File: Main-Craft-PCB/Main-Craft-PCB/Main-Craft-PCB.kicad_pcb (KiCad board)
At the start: 2 copper layers, 220 parts, among them J1 UART_1, J10 SOL_2, J11 PWR_IN, J12 SOL_3, J13 SOL_4, J14 Conn_01x10, J15 VESC_1, J16 VESC_2, J17 VESC_3, J18 VESC_4, J19 S500_1, J2 UART_2, J20 S500_2, J21 S500_3, J22 S500_4, J23 LEDS, J24 LEDS, J25 LEDS, J26 LEDS, J3 UART_3, J4 UART_4, J5 RELAY_1, J6 RELAY_2, J7 RELAY_3, J8 RELAY_3, J9 SOL_1, Q1 TIP120, Q10 S9013, Q11 S9013, Q12 S9013, Q13 S9013, Q14 S9013, Q15 IRFR9014PBF, Q16 S9013, Q2 TIP120, Q3 TIP120, Q4 TIP120, Q5 S9013, Q6 S9013, Q7 S9013, Q8 S9013, Q9 S9013, U1 74HC14, U10 ZSR330GTA, U11 ZLDO1117G50TA, U12 BFU590GX, U2 NUCLEO144-F429ZI, U3 ESP8266, U4 SN74LV4052, U5 LM358DR2G, U6 LM358DR2G, U7 LM358DR2G, U8 Pi Pico, U9 74HC14

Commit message: Start PCB Layout Place Most of Components
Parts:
- removed R57: 2K2, Resistor_SMD:R_0603_1608Metric
- removed R59: 10K, Resistor_SMD:R_0603_1608Metric
- removed RESET1: SW_SPST, Button_Switch_SMD:SW_Push_1P1T_NO_6x6mm_H9.5mm
- BTN_1: footprint My_library:12AWG_PWR_IN -> Button_Switch_SMD:SW_Push_1P1T_NO_6x6mm_H9.5mm
- C10, C11, C12, C13, C14, C15, C18, C19, C20, C21, C22, C23, C24, C25, C30, C31, C32, C35, C36, C37, D1, D13, D14, D15, D16, D17, D18, D2, D25, D26, D27, D3, D4, D5, D6, Q13, Q14, Q16, R10, R15, R16, R17, R18, R19, R2, R20, R27, R28, R29, R3, R30, R31, R32, R35, R36, R37, R38, R39, R4, R40, R5, R53, R54, R55, R56, R58, R6, R60, R61, R63, R64, R7, R8, R9, U1, U10, U11, U12, U5, U9: moved to B.Cu
- J10, J12, J13, J9: footprint My_library:Conn_01x03_MOLEX -> My_library:Conn_01x02_MOLEX
- J14: footprint Connector_PinHeader_1.27mm:PinHeader_1x10_P1.27mm_Vertical -> Connector_PinSocket_2.54mm:PinSocket_1x10_P2.54mm_Vertical
- moved J14 178.5 mm to (44.1, 93.0), turned to 0 degrees
- moved C26 172.1 mm to (53.4, 25.8)
- moved C27 172.1 mm to (55.9, 25.8)
- moved J1 166.9 mm to (179.8, 127.0), turned to -90 degrees
- moved RV6 162.7 mm to (282.3, 27.4)
- moved D31 162.1 mm to (82.3, 155.6), turned to 180 degrees
- moved RV3 161.1 mm to (273.6, 17.7)
- moved D28 160.6 mm to (78.7, 155.6), turned to 180 degrees
- moved D29 156.3 mm to (85.9, 155.6), turned to 180 degrees
- moved J2 155.6 mm to (179.8, 116.3), turned to -90 degrees
- moved RV4 153.6 mm to (271.5, 27.9)
- moved RV5 153.6 mm to (271.5, 22.9)
- moved RV1 153.6 mm to (265.9, 27.9)
- moved RV2 153.6 mm to (265.9, 22.9)
- moved RV7 153.6 mm to (277.1, 27.9)
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
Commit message: Continue PCB
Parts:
- C30, C31, C32, C35, C36, C37, D25, D26, D27, R53, R54, R55, U10, U11, U12: moved to F.Cu
- Q10, Q11, Q12, Q5, Q6, Q7, Q8, Q9, R25, R26, R33, R34, R41, R42, R43, R44, R45, R46, R47, R48, R49, R50, R51, R52: moved to B.Cu
- moved R26 171.2 mm to (187.8, 129.9)
- moved R41 168.7 mm to (185.3, 125.9)
- moved R42 166.4 mm to (182.8, 125.9)
- moved R43 164.1 mm to (180.3, 125.9)
- moved R44 162.0 mm to (177.8, 125.9)
- moved R45 160.0 mm to (175.3, 125.9)
- moved R46 158.1 mm to (172.8, 125.9)
- moved R47 156.3 mm to (170.2, 125.9)
- moved R34 154.8 mm to (167.7, 129.9)
- moved R48 154.8 mm to (167.7, 125.9)
- moved R50 152.0 mm to (162.7, 125.9)
- moved R52 149.9 mm to (157.7, 125.9)
- moved Q9 148.2 mm to (151.7, 119.2)
- moved RV11 148.0 mm to (140.1, 120.7), turned to 0 degrees
- moved Q12 148.0 mm to (138.4, 119.2)
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
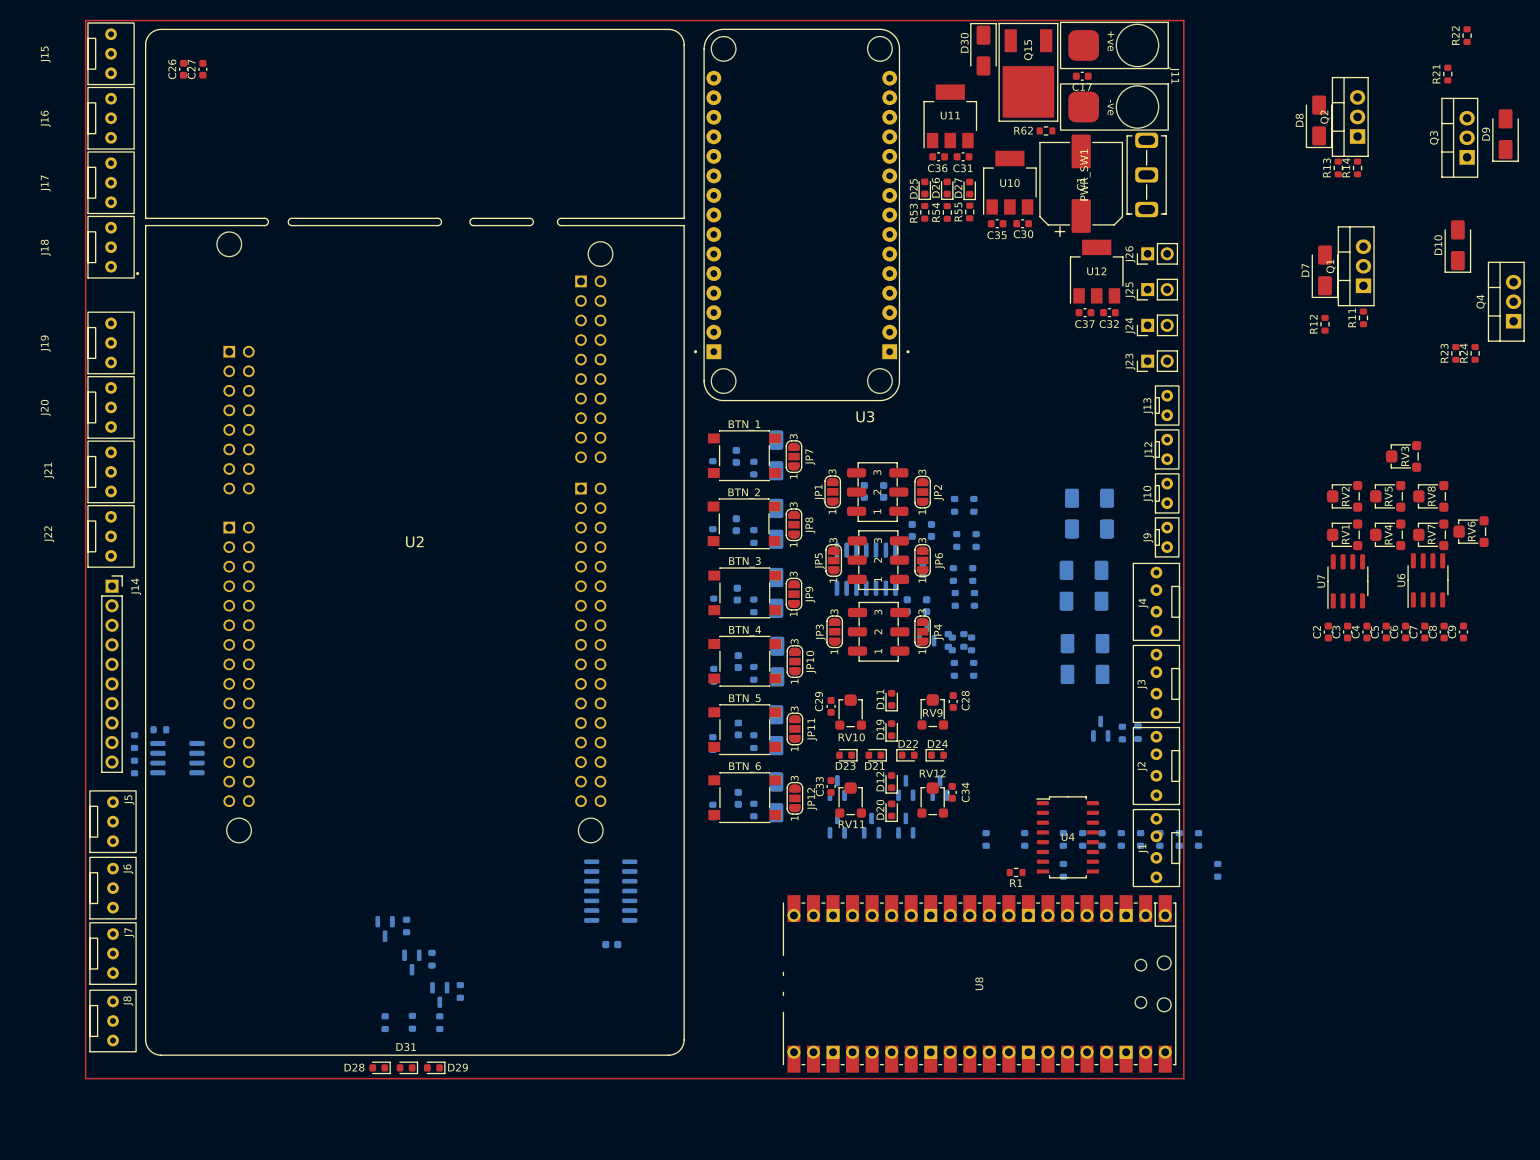
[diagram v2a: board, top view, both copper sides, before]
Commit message: Fix PCB schematic issues - start PCB again
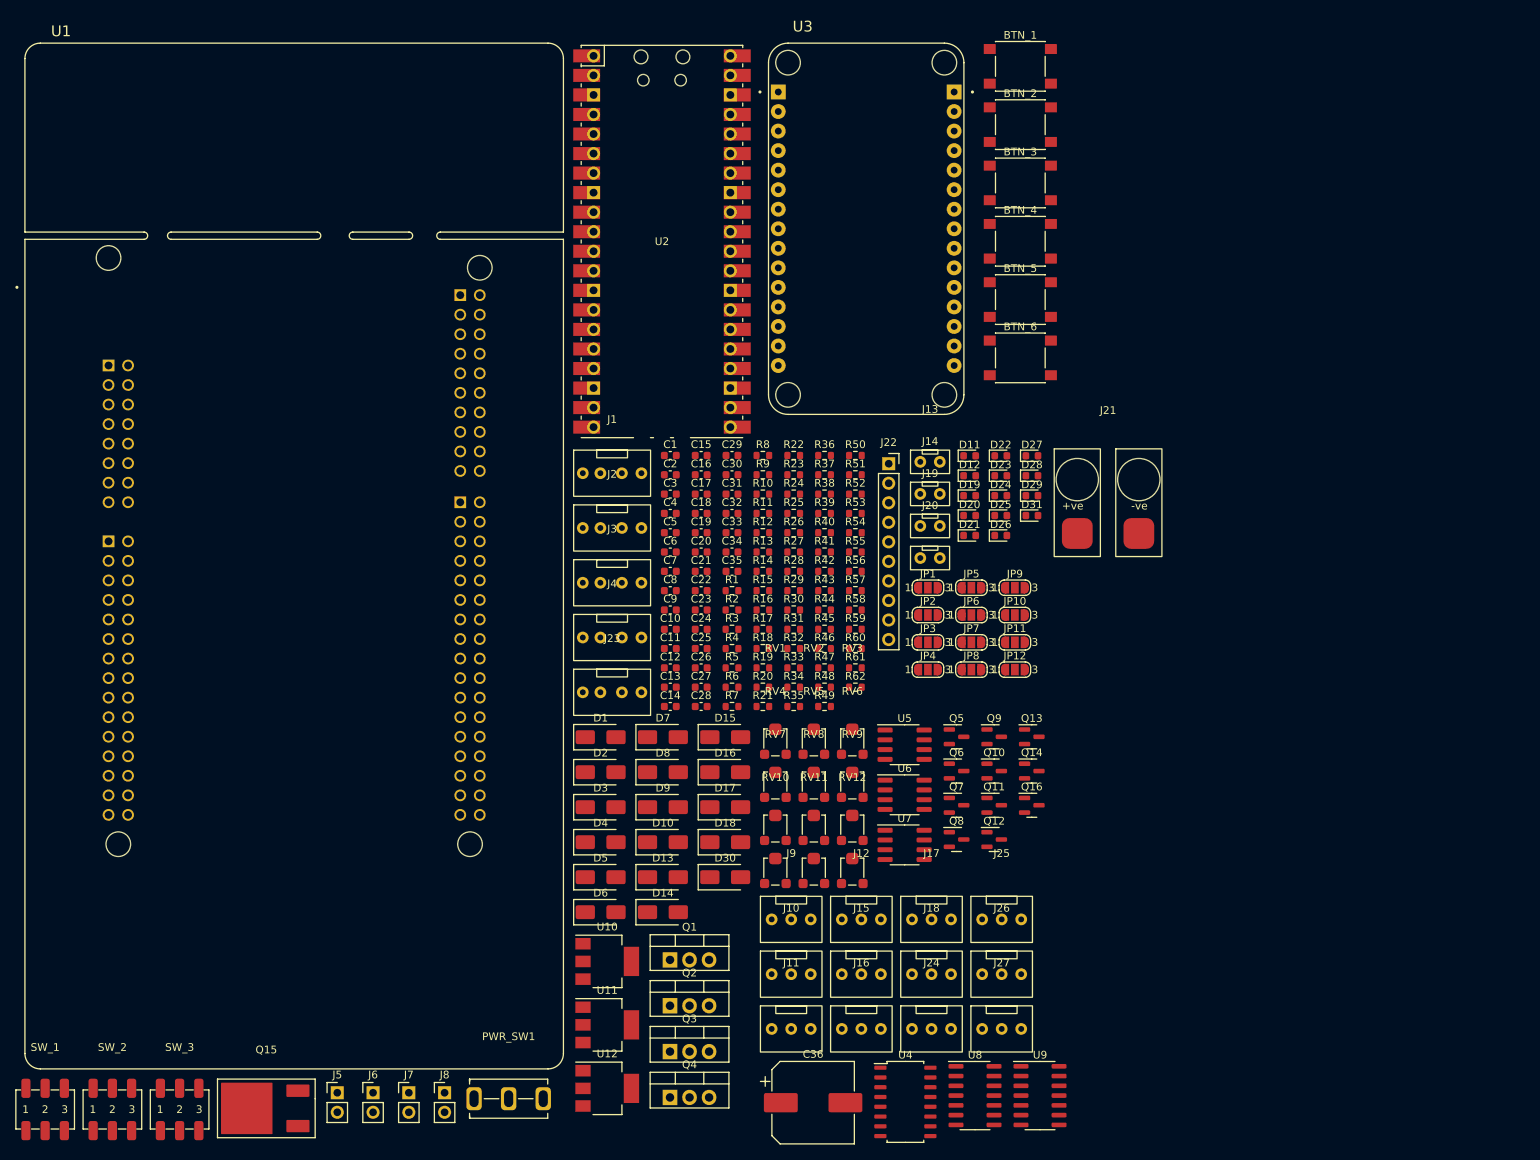
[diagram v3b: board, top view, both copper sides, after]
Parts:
- removed C37: 100nF, Capacitor_SMD:C_0603_1608Metric
- removed R63: 4K7, Resistor_SMD:R_0603_1608Metric
- removed R64: 1K, Resistor_SMD:R_0603_1608Metric
- added C16: 100nF, Capacitor_SMD:C_0603_1608Metric, F.Cu at (120.7, 78.5)
- added J27: VESC_4, My_library:Conn_01x03_MOLEX, F.Cu at (159.7, 150.5)
- added R57: 1K, Resistor_SMD:R_0603_1608Metric, F.Cu at (140.7, 93.5)
- added R59: 2K2, Resistor_SMD:R_0603_1608Metric, F.Cu at (140.7, 98.6)
- C1: value 470uF -> 100nF; footprint Capacitor_SMD:CP_Elec_10x10.5 -> Capacitor_SMD:C_0603_1608Metric
- C10, C11, C12, C13, C14, C15, C18, C19, C20, C21, C22, C23, C24, C25, D1, D13, D14, D15, D16, D17, D18, D2, D3, D4, D5, D6, Q10, Q11, Q12, Q13, Q14, Q16, Q5, Q6, Q7, Q8, Q9, R15, R16, R17, R18, R19, R25, R27, R28, R29, R30, R31, R33, R35, R36, R37, R38, R39, R40, R41, R42, R43, R44, R45, R46, R47, R48, R49, R5, R50, R51, R52, R56, R6, R7, R8, R9, U5, U9: moved to F.Cu
- C36: value 100nF -> 470uF; footprint Capacitor_SMD:C_0603_1608Metric -> Capacitor_SMD:CP_Elec_10x10.5
- J10: value SOL_2 -> S500_2; footprint My_library:Conn_01x02_MOLEX -> My_library:Conn_01x03_MOLEX
- J11: value PWR_IN -> S500_3; footprint My_library:12AWG_PWR_IN -> My_library:Conn_01x03_MOLEX
- J12: value SOL_3 -> S500_4; footprint My_library:Conn_01x02_MOLEX -> My_library:Conn_01x03_MOLEX
- J13: value SOL_4 -> SOL_1
- J14: value Conn_01x10 -> SOL_2; footprint Connector_PinSocket_2.54mm:PinSocket_1x10_P2.54mm_Vertical -> My_library:Conn_01x02_MOLEX
- J15: value VESC_1 -> RELAY_1
- J16: value VESC_2 -> RELAY_2
- J17: value VESC_3 -> RELAY_3
- J18: value VESC_4 -> RELAY_3
- J19: value S500_1 -> SOL_3; footprint My_library:Conn_01x03_MOLEX -> My_library:Conn_01x02_MOLEX
- J20: value S500_2 -> SOL_4; footprint My_library:Conn_01x03_MOLEX -> My_library:Conn_01x02_MOLEX
- J21: value S500_3 -> PWR_IN; footprint My_library:Conn_01x03_MOLEX -> My_library:12AWG_PWR_IN
- J22: value S500_4 -> Conn_01x10; footprint My_library:Conn_01x03_MOLEX -> Connector_PinSocket_2.54mm:PinSocket_1x10_P2.54mm_Vertical
- J23: value LEDS -> BAT_IN; footprint Connector_PinHeader_2.54mm:PinHeader_1x02_P2.54mm_Vertical -> My_library:Conn_01x04_MOLEX
- J24: value LEDS -> VESC_1; footprint Connector_PinHeader_2.54mm:PinHeader_1x02_P2.54mm_Vertical -> My_library:Conn_01x03_MOLEX
- J25: value LEDS -> VESC_2; footprint Connector_PinHeader_2.54mm:PinHeader_1x02_P2.54mm_Vertical -> My_library:Conn_01x03_MOLEX
- J26: value LEDS -> VESC_3; footprint Connector_PinHeader_2.54mm:PinHeader_1x02_P2.54mm_Vertical -> My_library:Conn_01x03_MOLEX
- J5: value RELAY_1 -> LEDS; footprint My_library:Conn_01x03_MOLEX -> Connector_PinHeader_2.54mm:PinHeader_1x02_P2.54mm_Vertical
- J6: value RELAY_2 -> LEDS; footprint My_library:Conn_01x03_MOLEX -> Connector_PinHeader_2.54mm:PinHeader_1x02_P2.54mm_Vertical
- J7, J8: value RELAY_3 -> LEDS; footprint My_library:Conn_01x03_MOLEX -> Connector_PinHeader_2.54mm:PinHeader_1x02_P2.54mm_Vertical
- J9: value SOL_1 -> S500_1; footprint My_library:Conn_01x02_MOLEX -> My_library:Conn_01x03_MOLEX
- R1: value 100K -> 1K
- R10, R20: value 47K -> 2K2; moved to F.Cu
- R11, R13, R21, R23: value 2K2 -> 47K
- R12, R22: value 47K -> 2K2
- R2: value 47K -> 1K; moved to F.Cu
- R24: value 47K -> 4K7
- R26: value 4K7 -> 47K; moved to F.Cu
- R3: value 1K -> 100K; moved to F.Cu
- R32: value 47K -> 150R; moved to F.Cu
- R34: value 150R -> 47K; moved to F.Cu
- R4: value 1K -> 47K; moved to F.Cu
- R58: value 1K -> 4K7; moved to F.Cu
- R60: value 4K7 -> 100R; moved to F.Cu
- R61: value 2K2 -> 4K7; moved to F.Cu
- R62: value 100R -> 1K
- U1: value 74HC14 -> NUCLEO144-F429ZI; footprint Package_SO:SO-14_3.9x8.65mm_P1.27mm -> My_library:MODULE_NUCLEO-F429ZI; moved to F.Cu
- U2: value NUCLEO144-F429ZI -> Pi Pico; footprint My_library:MODULE_NUCLEO-F429ZI -> My_library:pi_pico
- U8: value Pi Pico -> 74HC14; footprint My_library:Pi_Pico -> Package_SO:SO-14_3.9x8.65mm_P1.27mm
- moved Q15 166.7 mm to (61.6, 160.8), turned to 0 degrees
- moved Q3 155.7 mm to (116.6, 153.5), turned to 0 degrees
- moved J15 154.4 mm to (141.5, 143.4), turned to 0 degrees
- moved J16 153.4 mm to (141.5, 150.5), turned to 0 degrees
- moved Q4 149.0 mm to (116.6, 159.4), turned to 0 degrees
- moved PWR_SW1 145.9 mm to (95.6, 159.6), turned to 0 degrees
- moved Q2 144.1 mm to (116.6, 147.5), turned to 0 degrees
- moved J17 143.3 mm to (150.6, 136.3), turned to 0 degrees
- moved J18 142.5 mm to (150.6, 143.4), turned to 0 degrees
- moved D9 140.2 mm to (115.7, 121.7), turned to 0 degrees
- moved J11 130.8 mm to (132.4, 150.5), turned to 0 degrees
- moved SW_1 129.7 mm to (35.4, 161.0), turned to 0 degrees
- moved J21 129.7 mm to (173.5, 82.1), turned to 0 degrees
- moved D10 129.2 mm to (115.7, 126.2), turned to 0 degrees
- moved U11 126.2 mm to (108.4, 150.0), turned to 0 degrees
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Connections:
- C1 pad 1: VIN -> BATT_4_IN
- C10 pad 2: SW_2_UP_SB -> SW_2_DOWN_SB
- C11 pad 2: SW_2_DOWN_SB -> SW_3_UP_SB
- C12 pad 2: SW_3_UP_SB -> SW_3_DOWN_SB
- C13 pad 2: SW_3_DOWN_SB -> SW_1_UP_SB
- C14 pad 2: SW_1_UP_SB -> SW_1_DOWN_SB
- C15 pad 1: Earth -> +3V3
- C15 pad 2: SW_1_DOWN_SB -> Earth
- C17 pad 1: 12V_INPUT -> Earth
- C17 pad 2: Earth -> BTN_1_SB
- C18 pad 1: +3V3 -> Earth
- C18 pad 2: Earth -> BTN_2_SB
- C19 pad 2: BTN_1_SB -> BTN_3_SB
- C2 pad 1: BATT_4_IN -> BATT_3_IN
- C20 pad 2: BTN_2_SB -> BTN_4_SB
- C21 pad 2: BTN_3_SB -> BTN_5_SB
- C22 pad 2: BTN_4_SB -> BTN_6_SB
- C23 pad 1: Earth -> +3V3
- C23 pad 2: BTN_5_SB -> Earth
- C24 pad 1: Earth -> VESC_IN
- C24 pad 2: BTN_6_SB -> Earth
- C25 pad 1: +3V3 -> VESC_IN
- C26 pad 1: VESC_IN -> TRIM_POT_1
- C27 pad 1: VESC_IN -> TRIM_POT_3
- C28 pad 1: TRIM_POT_1 -> VIN
- C29 pad 1: TRIM_POT_3 -> VIN
- C3 pad 1: BATT_3_IN -> BATT_2_IN
- C31 pad 1: VIN -> TRIM_POT_2
- C32 pad 1: VIN -> TRIM_POT_4
- C33 pad 1: TRIM_POT_2 -> Earth
- C33 pad 2: Earth -> +3V3
- C34 pad 1: TRIM_POT_4 -> Earth
- C34 pad 2: Earth -> +5V
- C35 pad 2: +3V3 -> +12V
- C36 pad 1: Earth -> VIN
- C36 pad 2: +5V -> Earth
- C4 pad 1: BATT_2_IN -> BATT_1_IN
- C5 pad 1: BATT_1_IN -> +12V
- C9 pad 1: +12V -> Earth
- C9 pad 2: Earth -> SW_2_UP_SB
- J10 pad 1: +12V -> S500_2
- J10 pad 2: Net-(D8-A) -> +5V
- J11 pad 1: 12V_INPUT -> S500_3
- J11 pad 2: Earth -> +5V
- J12 pad 1: +12V -> S500_4
- J12 pad 2: Net-(D9-A) -> +5V
- J13 pad 2: Net-(D10-A) -> Net-(D7-A)
- J14 pad 1: VIN -> +12V
- J14 pad 2: MOSI_1 -> Net-(D8-A)
- J15 pad 1: VESC_IN_5V -> RELAY_1
- J15 pad 2: VESC_1 -> +5V
- J16 pad 1: VESC_IN_5V -> RELAY_2
- J16 pad 2: VESC_2 -> +5V
- J17 pad 1: VESC_IN_5V -> RELAY_3
- J17 pad 2: VESC_3 -> +5V
- J18 pad 1: VESC_IN_5V -> RELAY_4
- J18 pad 2: VESC_4 -> +5V
- J19 pad 1: S500_1 -> +12V
- J19 pad 2: +5V -> Net-(D9-A)
- J20 pad 1: S500_2 -> +12V
- J20 pad 2: +5V -> Net-(D10-A)
- J21 pad 1: S500_3 -> 12V_INPUT
- J21 pad 2: +5V -> Earth
- J22 pad 1: S500_4 -> VIN
- J22 pad 2: +5V -> MOSI_1
- J22 pad 3: Earth -> MISO_1
- J23 pad 1: +12V -> BATT_1_IN
- J23 pad 2: Earth -> BATT_2_IN
- J24 pad 1: +12V -> VESC_IN_5V
- J24 pad 2: Earth -> VESC_1
- J25 pad 1: +12V -> VESC_IN_5V
- J25 pad 2: Earth -> VESC_2
- J26 pad 1: +12V -> VESC_IN_5V
- J26 pad 2: Earth -> VESC_3
- J5 pad 1: RELAY_1 -> +12V
- J5 pad 2: +5V -> Earth
- J6 pad 1: RELAY_2 -> +12V
- J6 pad 2: +5V -> Earth
- J7 pad 1: RELAY_3 -> +12V
- J7 pad 2: +5V -> Earth
- J8 pad 1: RELAY_4 -> +12V
- J8 pad 2: +5V -> Earth
- J9 pad 1: +12V -> S500_1
- J9 pad 2: Net-(D7-A) -> +5V
- R1 pad 1: Earth -> Net-(U5A--)
- R1 pad 2: PICO_INH -> +12V
- R10 pad 1: Net-(D6-A) -> SOL_1
- R10 pad 2: +5V -> Net-(Q1-B)
- R11 pad 1: SOL_1 -> Earth
- R12 pad 1: Earth -> SOL_2
- R12 pad 2: Net-(Q1-B) -> Net-(Q2-B)
- R13 pad 1: SOL_2 -> Earth
- R14 pad 1: Earth -> SW_2_UP_SB
- R14 pad 2: Net-(Q2-B) -> Net-(D1-A)
- R15 pad 1: SW_2_UP_SB -> SW_2_DOWN_SB
- R15 pad 2: Net-(D1-A) -> Net-(D2-A)
- R16 pad 1: SW_2_DOWN_SB -> SW_3_UP_SB
- R16 pad 2: Net-(D2-A) -> Net-(D3-A)
- R17 pad 1: SW_3_UP_SB -> SW_3_DOWN_SB
- R17 pad 2: Net-(D3-A) -> Net-(D4-A)
- R18 pad 1: SW_3_DOWN_SB -> SW_1_UP_SB
- R18 pad 2: Net-(D4-A) -> Net-(D5-A)
- R19 pad 1: SW_1_UP_SB -> SW_1_DOWN_SB
- R19 pad 2: Net-(D5-A) -> Net-(D6-A)
- R2 pad 1: CON_CONNECTION -> Earth
- R2 pad 2: Earth -> Net-(U5A--)
- R20 pad 1: SW_1_DOWN_SB -> SOL_3
- R20 pad 2: Net-(D6-A) -> Net-(Q3-B)
- R21 pad 1: SOL_3 -> Earth
- R22 pad 1: Earth -> SOL_4
- R22 pad 2: Net-(Q3-B) -> Net-(Q4-B)
- R23 pad 1: SOL_4 -> Earth
- R24 pad 1: Earth -> Net-(Q5-B)
- R24 pad 2: Net-(Q4-B) -> SENS_1
- R25 pad 1: Net-(Q5-B) -> Net-(Q6-B)
- R25 pad 2: SENS_1 -> SENS_5
- R26 pad 1: Net-(Q6-B) -> Net-(BTN_1-B)
- R26 pad 2: SENS_5 -> +5V
- R27 pad 1: Net-(BTN_1-B) -> Net-(BTN_2-B)
- R28 pad 1: Net-(BTN_2-B) -> Net-(BTN_3-B)
- R29 pad 1: Net-(BTN_3-B) -> Net-(BTN_4-B)
- R3 pad 1: Net-(U5A--) -> Earth
- R3 pad 2: +12V -> PICO_INH
- R30 pad 1: Net-(BTN_4-B) -> Net-(BTN_5-B)
- R31 pad 1: Net-(BTN_5-B) -> Net-(BTN_6-B)
- R32 pad 1: Net-(BTN_6-B) -> Net-(Q5-C)
- R32 pad 2: +5V -> Net-(D11-K)
- R33 pad 1: Net-(Q5-C) -> Net-(Q6-C)
- R33 pad 2: Net-(D11-K) -> Net-(D12-K)
- R34 pad 1: Net-(Q6-C) -> BTN_1_SB
- R34 pad 2: Net-(D12-K) -> Net-(BTN_1-B)
- R35 pad 1: BTN_1_SB -> BTN_2_SB
- R35 pad 2: Net-(BTN_1-B) -> Net-(BTN_2-B)
- R36 pad 1: BTN_2_SB -> BTN_3_SB
- R36 pad 2: Net-(BTN_2-B) -> Net-(BTN_3-B)
- R37 pad 1: BTN_3_SB -> BTN_4_SB
- R37 pad 2: Net-(BTN_3-B) -> Net-(BTN_4-B)
- R38 pad 1: BTN_4_SB -> BTN_5_SB
- R38 pad 2: Net-(BTN_4-B) -> Net-(BTN_5-B)
- R39 pad 1: BTN_5_SB -> BTN_6_SB
- R39 pad 2: Net-(BTN_5-B) -> Net-(BTN_6-B)
- R4 pad 1: Earth -> Net-(D1-A)
- R4 pad 2: Net-(U5A--) -> +5V
- R40 pad 1: BTN_6_SB -> CON_CONNECTION
- R40 pad 2: Net-(BTN_6-B) -> Earth
- R5 pad 1: Net-(D1-A) -> Net-(D2-A)
- R58 pad 1: Net-(Q13-C) -> Net-(Q14-B)
- R58 pad 2: Net-(D28-K) -> DEBUG_2
- R6 pad 1: Net-(D2-A) -> Net-(D3-A)
- R60 pad 1: Net-(Q14-B) -> Net-(D30-A)
- R60 pad 2: DEBUG_2 -> Earth
- R61 pad 1: Net-(Q14-C) -> Net-(Q16-B)
- R61 pad 2: Net-(D29-K) -> DEBUG_3
- R62 pad 1: Net-(D30-A) -> Net-(Q16-C)
- R62 pad 2: Earth -> Net-(D31-K)
- R7 pad 1: Net-(D3-A) -> Net-(D4-A)
- R8 pad 1: Net-(D4-A) -> Net-(D5-A)
- R9 pad 1: Net-(D5-A) -> Net-(D6-A)
- SW_1 pad 1: Net-(D5-A) -> Net-(D1-A)
- SW_1 pad 3: Net-(D6-A) -> Net-(D2-A)
- SW_2 pad 1: Net-(D1-A) -> Net-(D3-A)
- SW_2 pad 3: Net-(D2-A) -> Net-(D4-A)
- SW_3 pad 1: Net-(D3-A) -> Net-(D5-A)
- SW_3 pad 3: Net-(D4-A) -> Net-(D6-A)
- U1 pad 1: BTN_1_SB -> SW_1_UP
- U1 pad 11: BTN_5_SB -> CLK_1
- U1 pad 12: BTN_6 -> unconnected-(U1-IOREF-Pad12)
- U1 pad 14: +3V3 -> RESET
- U1 pad 2: BTN_1 -> SW_1_DOWN
- U1 pad 3: BTN_2_SB -> SW_2_UP
- U1 pad 4: BTN_2 -> SW_2_DOWN
- U1 pad 8: BTN_4 -> Earth
- U2 pad 1: SW_1_UP -> PICO_TX
- U2 pad 11: CLK_1 -> I2C_PICO_SDA
- U2 pad 12: unconnected-(U2-IOREF-Pad12) -> I2C_PICO_SCl
- U2 pad 14: RESET -> unconnected-(U2-GP1O-Pad14)
- U2 pad 18: unconnected-(U2-+5V-Pad18) -> Earth
- U2 pad 19: Earth -> unconnected-(U2-GP14-Pad19)
- U2 pad 2: SW_1_DOWN -> PICO_RX
- U2 pad 20: Earth -> unconnected-(U2-GP15-Pad20)
- U2 pad 24: +12V -> unconnected-(U2-GP18-Pad24)
- U2 pad 28: LOW_VOLT_3 -> Earth
- U2 pad 3: SW_2_UP -> Earth
- U2 pad 32: TRIM_POT_1 -> unconnected-(U2-GP27-Pad32)
- U2 pad 38: BTN_1 -> Earth
- U2 pad 39: BTN_5 -> +3V3
- U2 pad 4: SW_2_DOWN -> PICO_INH
- U2 pad 40: BTN_6 -> unconnected-(U2-VBUS-Pad40)
- U8 pad 1: PICO_TX -> SW_1_UP_SB
- U8 pad 10: unconnected-(U8-GP7-Pad10) -> SW_3_UP
- U8 pad 11: I2C_PICO_SDA -> SW_3_UP_SB
- U8 pad 12: I2C_PICO_SCl -> SW_3_DOWN
- U8 pad 13: Earth -> SW_3_DOWN_SB
- U8 pad 14: unconnected-(U8-GP1O-Pad14) -> +3V3
- U8 pad 2: PICO_RX -> SW_1_UP
- U8 pad 3: Earth -> SW_1_DOWN_SB
- U8 pad 4: PICO_INH -> SW_1_DOWN
- U8 pad 5: UART_EN_A -> SW_2_UP_SB
- U8 pad 6: UART_EN_B -> SW_2_UP
- U8 pad 7: unconnected-(U8-GP5-Pad7) -> Earth
- U8 pad 8: Earth -> SW_2_DOWN
- U8 pad 9: unconnected-(U8-GP6-Pad9) -> SW_2_DOWN_SB
- U9 pad 1: SW_1_UP_SB -> BTN_1_SB
- U9 pad 10: SW_3_UP -> BTN_5
- U9 pad 11: SW_3_UP_SB -> BTN_5_SB
- U9 pad 12: SW_3_DOWN -> BTN_6
- U9 pad 13: SW_3_DOWN_SB -> BTN_6_SB
- U9 pad 2: SW_1_UP -> BTN_1
- U9 pad 3: SW_1_DOWN_SB -> BTN_2_SB
- U9 pad 4: SW_1_DOWN -> BTN_2
- U9 pad 5: SW_2_UP_SB -> BTN_3_SB
- U9 pad 6: SW_2_UP -> BTN_3
- U9 pad 8: SW_2_DOWN -> BTN_4
- U9 pad 9: SW_2_DOWN_SB -> BTN_4_SB
